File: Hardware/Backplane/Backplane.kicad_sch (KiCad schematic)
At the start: 9 parts, among them J1 10018784-10201TLF

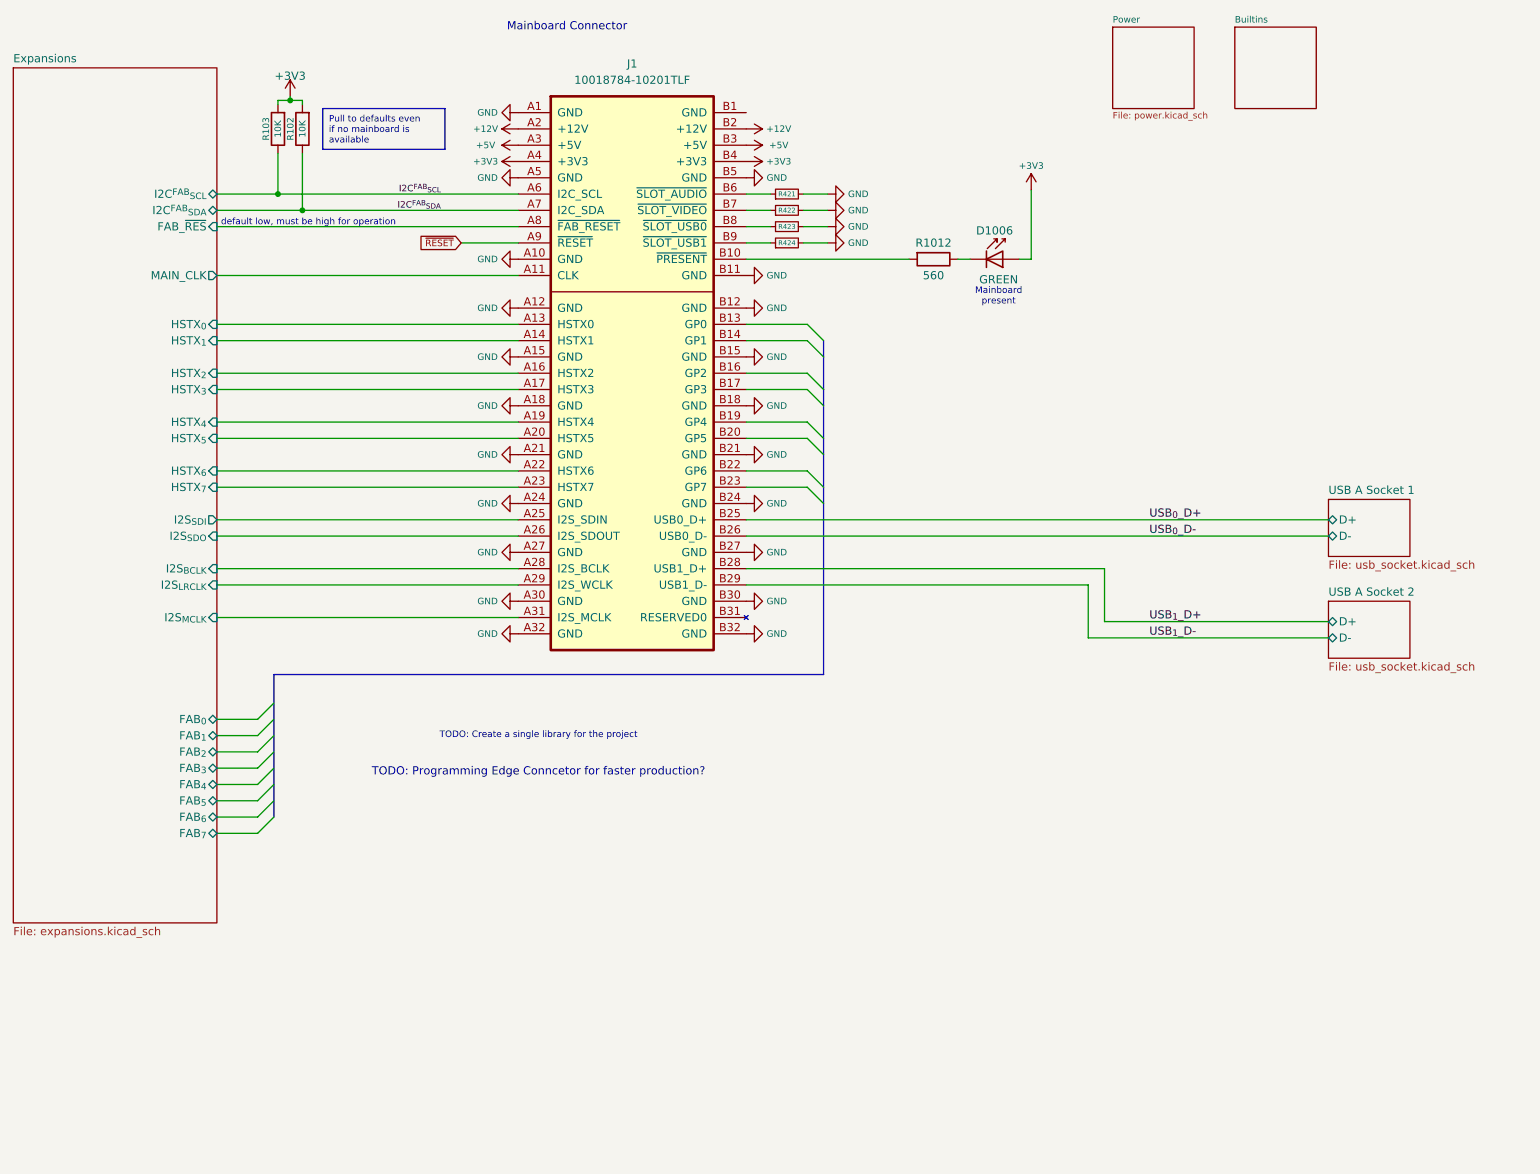
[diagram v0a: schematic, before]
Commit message: Fixes two issues regarding the power supply of the TCA9548APWR, routes TCA9548APWR.RESET to the main board controller.
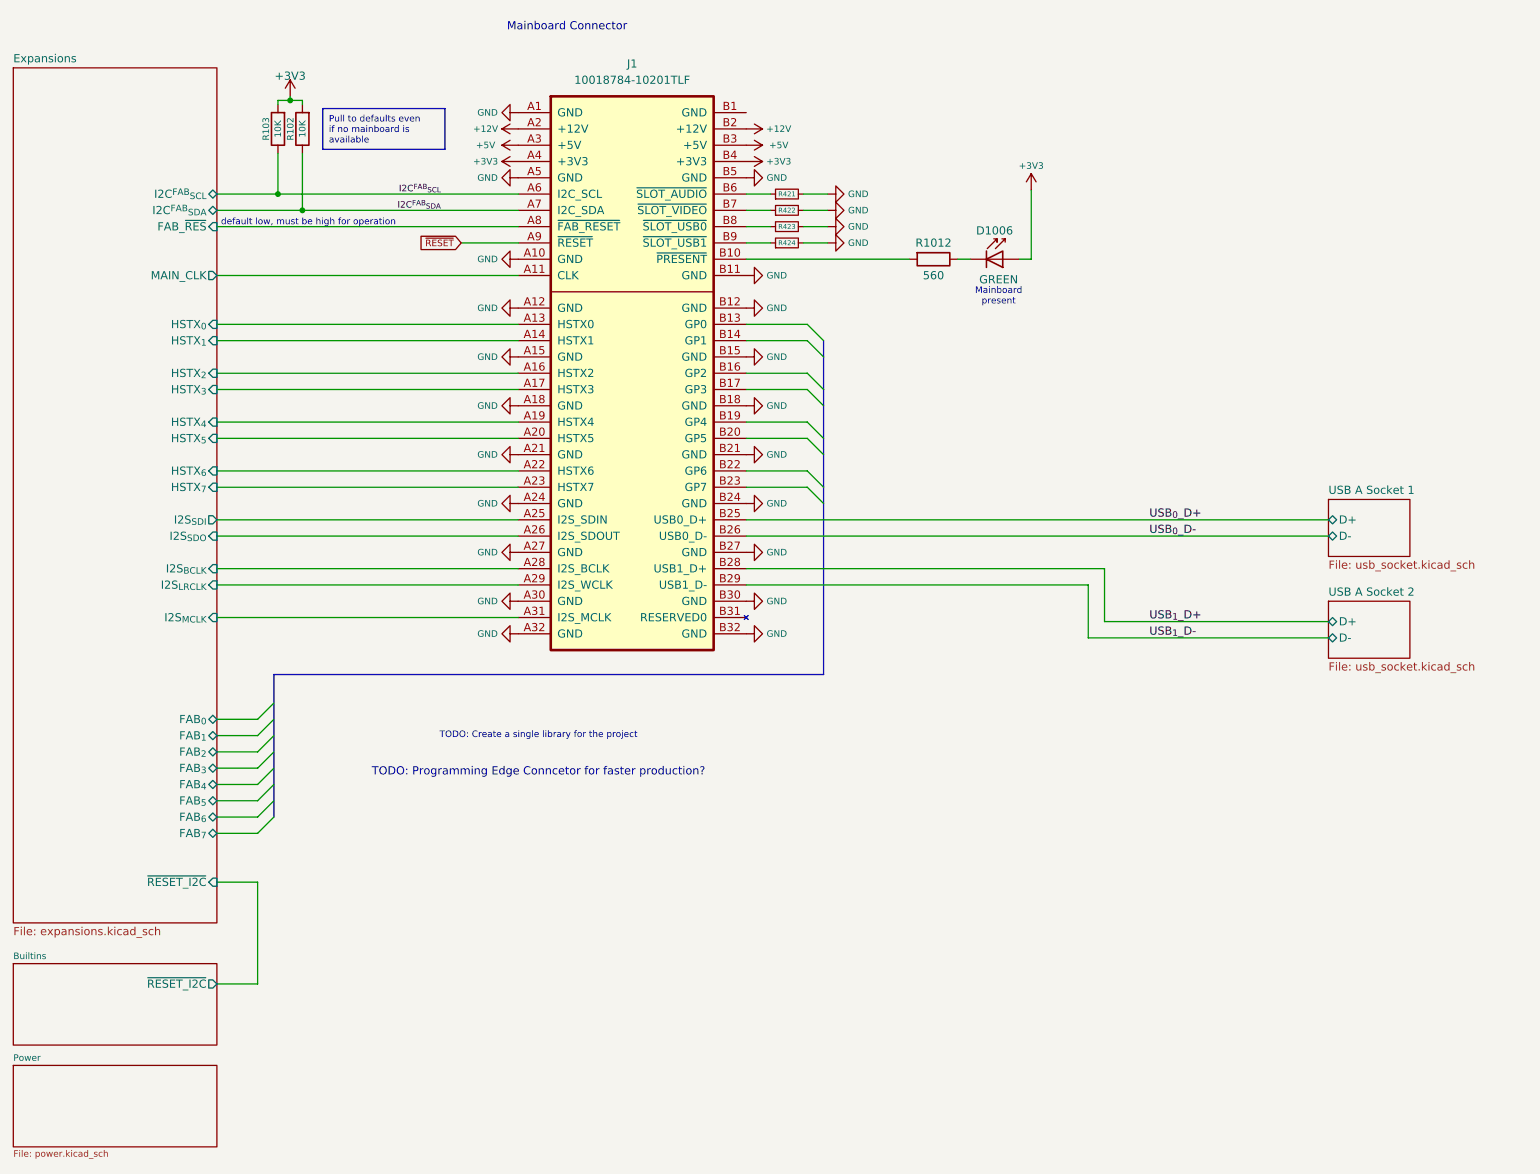
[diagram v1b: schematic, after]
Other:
- sheet Builtins ports: added ~{RESET_I2C}; removed none
- sheet Expansions ports: added ~{RESET_I2C}; removed none
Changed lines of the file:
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@@
 	(wire
 		(pts
+			(xy 76.2 168.275) (xy 82.55 168.275)
+		)
+		(stroke
+			(width 0)
+			(type default)
+		)
+	)
+	(wire
+		(pts
 			(xy 212.09 114.3) (xy 249.555 114.3)
 		)
@@
 	(wire
 		(pts
+			(xy 82.55 168.275) (xy 82.55 152.4)
+		)
+		(stroke
+			(width 0)
+			(type default)
+		)
+	)
+	(wire
+		(pts
 			(xy 85.725 30.48) (xy 87.63 30.48)
 		)
@@
 	(wire
 		(pts
+			(xy 76.2 152.4) (xy 82.55 152.4)
+		)
+		(stroke
+			(width 0)
+			(type default)
+		)
+	)
+	(wire
+		(pts
 			(xy 76.2 95.885) (xy 123.19 95.885)
 		)
@@
 	)
 	(sheet
-		(at 234.95 19.05)
-		(size 12.7 12.7)
+		(at 44.45 165.1)
+		(size 31.75 12.7)
 		(exclude_from_sim no)
 		(in_bom yes)
@@
 		)
 		(property "Sheetname" "Builtins"
-			(at 234.95 18.4654 0)
+			(at 44.45 164.5154 0)
 			(show_name no)
 			(do_not_autoplace no)
@@
 		)
 		(property "Sheetfile" "builtins.kicad_sch"
-			(at 234.95 32.233 0)
+			(at 44.45 178.283 0)
 			(hide yes)
 			(show_name no)
@@
 			)
 		)
+		(pin "~{RESET_I2C}" output
+			(at 76.2 168.275 0)
+			(effects
+				(font
+					(size 1.27 1.27)
+				)
+				(justify right)
+			)
+		)
 		(instances
 			(project "Backplane"
@@
 	)
 	(sheet
-		(at 215.9 19.05)
-		(size 12.7 12.7)
+		(at 44.45 180.975)
+		(size 31.75 12.7)
 		(exclude_from_sim no)
 		(in_bom yes)
@@
 		)
 		(property "Sheetname" "Power"
-			(at 215.9 18.4654 0)
+			(at 44.45 180.3904 0)
 			(show_name no)
 			(do_not_autoplace no)
@@
 		)
 		(property "Sheetfile" "power.kicad_sch"
-			(at 215.9 32.233 0)
+			(at 44.45 194.158 0)
 			(show_name no)
 			(do_not_autoplace no)
@@
 			(effects
 				(font
+					(size 1.27 1.27)
+				)
+				(justify right)
+			)
+		)
+		(pin "~{RESET_I2C}" input
+			(at 76.2 152.4 0)
+			(effects
+				(font
